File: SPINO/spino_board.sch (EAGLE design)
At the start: 22 parts, among them IC1 ATMEGA168-20P, Q1 16M

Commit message: done SPINO
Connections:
- removed net N$32: C2.2, IC1.AREF, JP4.8, RESET.P, RESET.P1
- new net N$2: IC1.AREF, JP4.7
- net GND: now also C2.2, JP4.8, RESET.P, RESET.P1; no longer JP4.7
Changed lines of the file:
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@@
 <setting verticaltext="up"/>
 </settings>
-<grid distance="0.1" unitdist="inch" unit="inch" style="lines" multiple="1" display="no" altdistance="0.01" altunitdist="inch" altunit="mil"/>
+<grid distance="50" unitdist="mil" unit="mil" style="lines" multiple="1" display="yes" altdistance="0.01" altunitdist="inch" altunit="mil"/>
 <layers>
 <layer number="1" name="Top" color="4" fill="1" visible="no" active="no"/>
@@
 <part name="R6" library="datle-discrete" deviceset="R-US_" device="0207/10" value="330"/>
 <part name="GND9" library="supply1" deviceset="GND" device=""/>
+<part name="GND10" library="supply1" deviceset="GND" device=""/>
 </parts>
 <sheets>
@@
 <instance part="JP3" gate="A" x="212.09" y="87.63"/>
 <instance part="JP4" gate="A" x="212.09" y="64.77"/>
-<instance part="GND6" gate="1" x="106.68" y="62.23"/>
+<instance part="GND6" gate="1" x="106.68" y="59.69"/>
 <instance part="C5" gate="G$1" x="115.57" y="83.82" smashed="yes" rot="R270">
 <attribute name="NAME" x="116.586" y="80.899" size="1.778" layer="95" rot="R180"/>
@@
 </instance>
 <instance part="GND9" gate="1" x="223.52" y="27.94"/>
+<instance part="GND10" gate="1" x="102.87" y="59.69"/>
 </instances>
 <busses>
@@
 <segment>
 <pinref part="GND6" gate="1" pin="GND"/>
-<wire x1="106.68" y1="64.77" x2="106.68" y2="83.82" width="0.1524" layer="91"/>
+<wire x1="106.68" y1="62.23" x2="106.68" y2="83.82" width="0.1524" layer="91"/>
 <pinref part="C3" gate="G$1" pin="2"/>
 <wire x1="106.68" y1="83.82" x2="106.68" y2="92.71" width="0.1524" layer="91"/>
@@
 </segment>
 <segment>
-<pinref part="JP4" gate="A" pin="7"/>
-<wire x1="209.55" y1="59.69" x2="203.2" y2="59.69" width="0.1524" layer="91"/>
-<wire x1="203.2" y1="59.69" x2="203.2" y2="52.07" width="0.1524" layer="91"/>
-<pinref part="GND7" gate="1" pin="GND"/>
-</segment>
-<segment>
 <pinref part="GND8" gate="1" pin="GND"/>
 <wire x1="201.93" y1="135.89" x2="201.93" y2="138.43" width="0.1524" layer="91"/>
@@
 <wire x1="219.71" y1="35.56" x2="223.52" y2="35.56" width="0.1524" layer="91"/>
 <wire x1="223.52" y1="35.56" x2="223.52" y2="30.48" width="0.1524" layer="91"/>
+</segment>
+<segment>
+<pinref part="JP4" gate="A" pin="8"/>
+<pinref part="GND7" gate="1" pin="GND"/>
+<wire x1="209.55" y1="57.15" x2="203.2" y2="57.15" width="0.1524" layer="91"/>
+<wire x1="203.2" y1="57.15" x2="203.2" y2="52.07" width="0.1524" layer="91"/>
+</segment>
+<segment>
+<pinref part="RESET" gate="1" pin="P1"/>
+<pinref part="RESET" gate="1" pin="P"/>
+<wire x1="102.87" y1="123.19" x2="102.87" y2="62.23" width="0.1524" layer="91"/>
+<pinref part="C2" gate="G$1" pin="2"/>
+<wire x1="106.68" y1="123.19" x2="102.87" y2="123.19" width="0.1524" layer="91"/>
+<wire x1="102.87" y1="129.54" x2="102.87" y2="127" width="0.1524" layer="91"/>
+<wire x1="102.87" y1="127" x2="102.87" y2="123.19" width="0.1524" layer="91"/>
+<wire x1="105.41" y1="129.54" x2="102.87" y2="129.54" width="0.1524" layer="91"/>
+<wire x1="105.41" y1="127" x2="102.87" y2="127" width="0.1524" layer="91"/>
+<junction x="102.87" y="123.19"/>
+<junction x="102.87" y="127"/>
+<pinref part="GND10" gate="1" pin="GND"/>
 </segment>
 </net>
@@
 </segment>
 </net>
-<net name="N$32" class="0">
-<segment>
-<pinref part="RESET" gate="1" pin="P1"/>
-<pinref part="RESET" gate="1" pin="P"/>
-<pinref part="IC1" gate="G$1" pin="AREF"/>
-<wire x1="129.54" y1="115.57" x2="102.87" y2="115.57" width="0.1524" layer="91"/>
-<wire x1="102.87" y1="115.57" x2="102.87" y2="57.15" width="0.1524" layer="91"/>
-<pinref part="JP4" gate="A" pin="8"/>
-<wire x1="102.87" y1="57.15" x2="209.55" y2="57.15" width="0.1524" layer="91"/>
-<pinref part="C2" gate="G$1" pin="2"/>
-<wire x1="106.68" y1="123.19" x2="102.87" y2="123.19" width="0.1524" layer="91"/>
-<wire x1="102.87" y1="123.19" x2="102.87" y2="115.57" width="0.1524" layer="91"/>
-<wire x1="102.87" y1="129.54" x2="102.87" y2="127" width="0.1524" layer="91"/>
-<wire x1="102.87" y1="127" x2="102.87" y2="123.19" width="0.1524" layer="91"/>
-<wire x1="105.41" y1="129.54" x2="102.87" y2="129.54" width="0.1524" layer="91"/>
-<wire x1="105.41" y1="127" x2="102.87" y2="127" width="0.1524" layer="91"/>
-<junction x="102.87" y="123.19"/>
-<junction x="102.87" y="127"/>
-<junction x="102.87" y="115.57"/>
-</segment>
-</net>
 <net name="N$14" class="0">
 <segment>
@@
 </segment>
 </net>
+<net name="N$2" class="0">
+<segment>
+<pinref part="IC1" gate="G$1" pin="AREF"/>
+<wire x1="129.54" y1="115.57" x2="93.98" y2="115.57" width="0.1524" layer="91"/>
+<wire x1="93.98" y1="115.57" x2="93.98" y2="59.69" width="0.1524" layer="91"/>
+<pinref part="JP4" gate="A" pin="7"/>
+<wire x1="93.98" y1="59.69" x2="209.55" y2="59.69" width="0.1524" layer="91"/>
+</segment>
+</net>

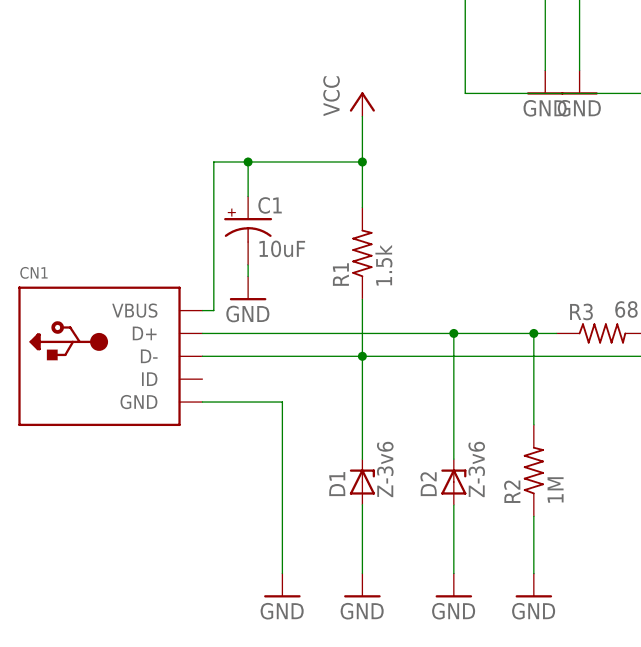
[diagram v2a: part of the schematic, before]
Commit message: SPINO usb done
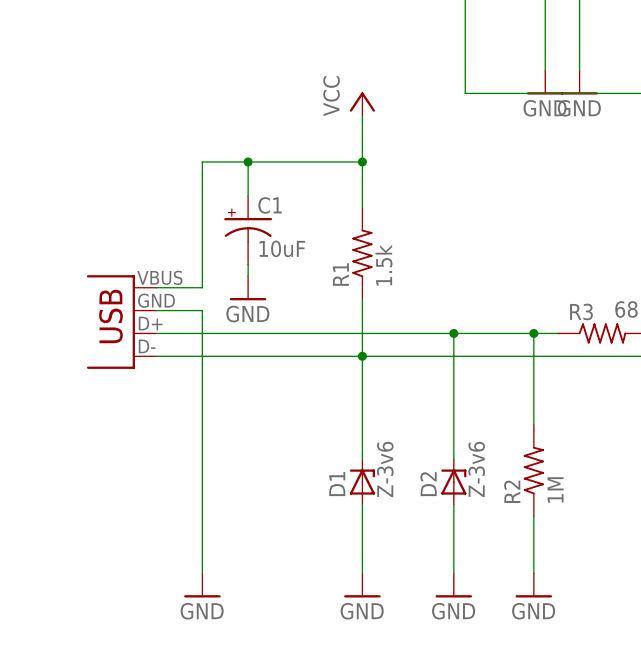
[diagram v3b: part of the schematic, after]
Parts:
- CN1: value (none) -> USB-2-A-H; device datle-conn:USBMINIB -> datle-conn:USB-2-A-H
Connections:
- net GND: now also CN1.VBUS; no longer CN1.GND
- net N$3: now also CN1.D+; no longer CN1.D-
- net N$4: now also CN1.D-; no longer CN1.D+
- net VCC: now also CN1.GND; no longer CN1.VBUS
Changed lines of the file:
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@@
 <setting verticaltext="up"/>
 </settings>
-<grid distance="0.1" unitdist="inch" unit="inch" style="lines" multiple="1" display="no" altdistance="0.01" altunitdist="inch" altunit="inch"/>
+<grid distance="50" unitdist="mil" unit="mil" style="lines" multiple="1" display="yes" altdistance="0.01" altunitdist="inch" altunit="mil"/>
 <layers>
 <layer number="1" name="Top" color="4" fill="1" visible="no" active="no"/>
@@
 <part name="D1" library="datle-discrete" deviceset="Z-5V1" device="" value="Z-3v6"/>
 <part name="D2" library="datle-discrete" deviceset="Z-5V1" device="" value="Z-3v6"/>
-<part name="CN1" library="datle-conn" deviceset="USB" device="MINIB"/>
+<part name="CN1" library="datle-conn" deviceset="USB-2" device="-A-H"/>
 <part name="GND1" library="supply1" deviceset="GND" device=""/>
 <part name="GND2" library="supply1" deviceset="GND" device=""/>
@@
 <instance part="D1" gate="Z5V1" x="82.55" y="16.51" rot="R90"/>
 <instance part="D2" gate="Z5V1" x="92.71" y="16.51" rot="R90"/>
-<instance part="CN1" gate="G$1" x="54.61" y="30.48"/>
-<instance part="GND1" gate="1" x="73.66" y="3.81"/>
+<instance part="CN1" gate="G$1" x="57.15" y="38.1" rot="R180"/>
+<instance part="GND1" gate="1" x="64.77" y="3.81"/>
 <instance part="GND2" gate="1" x="82.55" y="3.81"/>
 <instance part="GND3" gate="1" x="92.71" y="3.81"/>
@@
 <net name="GND" class="0">
 <segment>
-<pinref part="CN1" gate="G$1" pin="GND"/>
 <pinref part="GND1" gate="1" pin="GND"/>
-<wire x1="64.77" y1="25.4" x2="73.66" y2="25.4" width="0.1524" layer="91"/>
-<wire x1="73.66" y1="25.4" x2="73.66" y2="6.35" width="0.1524" layer="91"/>
+<wire x1="64.77" y1="35.56" x2="64.77" y2="6.35" width="0.1524" layer="91"/>
+<pinref part="CN1" gate="G$1" pin="VBUS"/>
+<wire x1="59.69" y1="35.56" x2="64.77" y2="35.56" width="0.1524" layer="91"/>
 </segment>
 <segment>
@@
 <pinref part="D1" gate="Z5V1" pin="C"/>
 <wire x1="82.55" y1="36.83" x2="82.55" y2="30.48" width="0.1524" layer="91"/>
-<pinref part="CN1" gate="G$1" pin="D-"/>
 <wire x1="82.55" y1="30.48" x2="82.55" y2="19.05" width="0.1524" layer="91"/>
-<wire x1="64.77" y1="30.48" x2="82.55" y2="30.48" width="0.1524" layer="91"/>
 <pinref part="R4" gate="G$1" pin="1"/>
 <wire x1="82.55" y1="30.48" x2="114.3" y2="30.48" width="0.1524" layer="91"/>
 <junction x="82.55" y="30.48"/>
+<pinref part="CN1" gate="G$1" pin="D+"/>
+<wire x1="59.69" y1="30.48" x2="82.55" y2="30.48" width="0.1524" layer="91"/>
 </segment>
 </net>
 <net name="N$4" class="0">
 <segment>
-<pinref part="CN1" gate="G$1" pin="D+"/>
-<wire x1="64.77" y1="33.02" x2="92.71" y2="33.02" width="0.1524" layer="91"/>
 <pinref part="D2" gate="Z5V1" pin="C"/>
 <wire x1="92.71" y1="33.02" x2="101.6" y2="33.02" width="0.1524" layer="91"/>
@@
 <pinref part="R3" gate="G$1" pin="1"/>
 <wire x1="101.6" y1="33.02" x2="104.14" y2="33.02" width="0.1524" layer="91"/>
+<junction x="101.6" y="33.02"/>
+<pinref part="CN1" gate="G$1" pin="D-"/>
+<wire x1="59.69" y1="33.02" x2="92.71" y2="33.02" width="0.1524" layer="91"/>
 <junction x="92.71" y="33.02"/>
-<junction x="101.6" y="33.02"/>
 </segment>
 </net>
@@
 <wire x1="69.85" y1="48.26" x2="69.85" y2="52.07" width="0.1524" layer="91"/>
 <junction x="69.85" y="52.07"/>
-<pinref part="CN1" gate="G$1" pin="VBUS"/>
-<wire x1="66.04" y1="35.56" x2="64.77" y2="35.56" width="0.1524" layer="91"/>
-<wire x1="66.04" y1="52.07" x2="66.04" y2="35.56" width="0.1524" layer="91"/>
-<wire x1="66.04" y1="52.07" x2="69.85" y2="52.07" width="0.1524" layer="91"/>
-</segment>
-<segment>
+<wire x1="64.77" y1="52.07" x2="69.85" y2="52.07" width="0.1524" layer="91"/>
+<pinref part="CN1" gate="G$1" pin="GND"/>
+<wire x1="59.69" y1="38.1" x2="64.77" y2="38.1" width="0.1524" layer="91"/>
+<wire x1="64.77" y1="38.1" x2="64.77" y2="52.07" width="0.1524" layer="91"/>
+</segment>
+<segment>
